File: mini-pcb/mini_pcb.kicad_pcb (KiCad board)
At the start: 4 copper layers, 0 parts

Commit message: mini-pcb layout
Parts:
- added A1: Electrosmith_Daisy_Seed_Rev4, Module:Electrosmith_Daisy_Seed, B.Cu at (122.5, 132.3)
- added C1: 10UF, Capacitor_SMD:C_0805_2012Metric, F.Cu at (111.1, 116.6)
- added C10: 10uf, Capacitor_SMD:C_0805_2012Metric, F.Cu at (139.2, 135.2)
- added C2: 10uf, Capacitor_SMD:C_0805_2012Metric, F.Cu at (153.8, 143.4)
- added C3: 10uf, Capacitor_SMD:C_0805_2012Metric, F.Cu at (163.0, 129.0)
- added C4: 10UF, Capacitor_SMD:C_0805_2012Metric, F.Cu at (111.1, 114.6)
- added C5: 10uf, Capacitor_SMD:C_0805_2012Metric, F.Cu at (168.8, 129.0)
- added C6: 10uf, Capacitor_SMD:C_0805_2012Metric, F.Cu at (153.7, 136.3)
- added C7: 0.1uf, Capacitor_SMD:C_0805_2012Metric, F.Cu at (107.5, 116.6)
- added C8: 0.1uf, Capacitor_SMD:C_0805_2012Metric, F.Cu at (107.5, 114.6)
- added C9: 10uf, Capacitor_SMD:C_0805_2012Metric, F.Cu at (139.2, 144.6)
- added D1: 1N5817, Diode_SMD:D_SOD-123, F.Cu at (105.3, 120.1)
- added J3: Barrel_Jack_Switch, Connector_BarrelJack:BarrelJack_Horizontal, B.Cu at (99.5, 127.8)
- added J4: AUDIO_IN_TRS, Connector_Audio:Jack_6.35mm_Neutrik_NMJ6HCD3_Horizontal, F.Cu at (181.5, 131.8)
- added J5: AUDIO_OUT_TRS, Connector_Audio:Jack_6.35mm_Neutrik_NMJ6HCD3_Horizontal, F.Cu at (111.0, 148.1)
- added R1: 1M, Resistor_SMD:R_0603_1608Metric, F.Cu at (154.2, 138.8)
- added R10: 1M, Resistor_SMD:R_0603_1608Metric, F.Cu at (154.2, 140.9)
- added R11: 1M, Resistor_SMD:R_0603_1608Metric, F.Cu at (162.2, 125.8)
- added R12: 1M, Resistor_SMD:R_0603_1608Metric, F.Cu at (163.8, 125.8)
- added R13: 1M, Resistor_SMD:R_0603_1608Metric, F.Cu at (139.8, 137.8)
- added R14: 1M, Resistor_SMD:R_0603_1608Metric, F.Cu at (137.5, 135.2)
- added R2: 1M, Resistor_SMD:R_0603_1608Metric, F.Cu at (155.5, 136.3)
- added R3: 1M, Resistor_SMD:R_0603_1608Metric, F.Cu at (169.5, 125.8)
- added R4: 1M, Resistor_SMD:R_0603_1608Metric, F.Cu at (168.0, 125.8)
- added R5: 1M, Resistor_SMD:R_0603_1608Metric, F.Cu at (139.8, 142.1)
- added R6: 1M, Resistor_SMD:R_0603_1608Metric, F.Cu at (158.8, 136.0)
- added R7: 1M, Resistor_SMD:R_0603_1608Metric, F.Cu at (158.8, 137.5)
- added R8: 1M, Resistor_SMD:R_0603_1608Metric, F.Cu at (137.5, 144.6)
- added R9: 1M, Resistor_SMD:R_0603_1608Metric, F.Cu at (155.5, 143.4)
- added U1: LM1117DT-5.0, Package_TO_SOT_SMD:TO-252-3_TabPin2, F.Cu at (110.0, 124.1)
- added U2: OPA1664D, Package_SO:SOIC-14_3.9x8.7mm_P1.27mm, F.Cu at (148.5, 140.0)
- added U3: OPA1655DBV, Package_TO_SOT_SMD:SOT-23-5, F.Cu at (158.5, 140.0)
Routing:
- net AUDIO_IN_JACK_RIGHT: track 0.00 -> 75.9 mm
- net AUDIO_OUT_JACK_RIGHT: track 0.00 -> 40.3 mm
- net unconnected-(A1-SPI1_SCK-Pad9): track 0.00 -> 38.4 mm
- net +3.3V: track 38.4 -> 0.00 mm
- net Net-(BT1-+): track 36.6 -> 0.00 mm
- net AUDIO_OUT_JACK_LEFT: track 0.00 -> 29.4 mm
- net AUDIO_IN_JACK_LEFT: track 0.00 -> 29.4 mm
- net +2.5V: track 0.00 -> 10.5 mm
- net DGND: track 0.00 -> 9.58 mm, vias 0 -> 7
- net Net-(U2C--): track 0.00 -> 8.69 mm, vias 0 -> 2
- net Net-(U2D--): track 0.00 -> 8.68 mm
- net +5V: track 0.00 -> 6.78 mm
- net Net-(U2A-+): track 0.00 -> 4.27 mm
- net Net-(U2B-+): track 0.00 -> 4.12 mm
- net Net-(U3-+): track 0.00 -> 3.07 mm
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- added copper zone on In1.Cu, net (none)
- added copper zone on In2.Cu, net (none)
- removed copper zone on In2.Cu, net +3.3V
- removed copper zone on In1.Cu, net GND
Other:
- board outline added: 110 x 22.2 mm

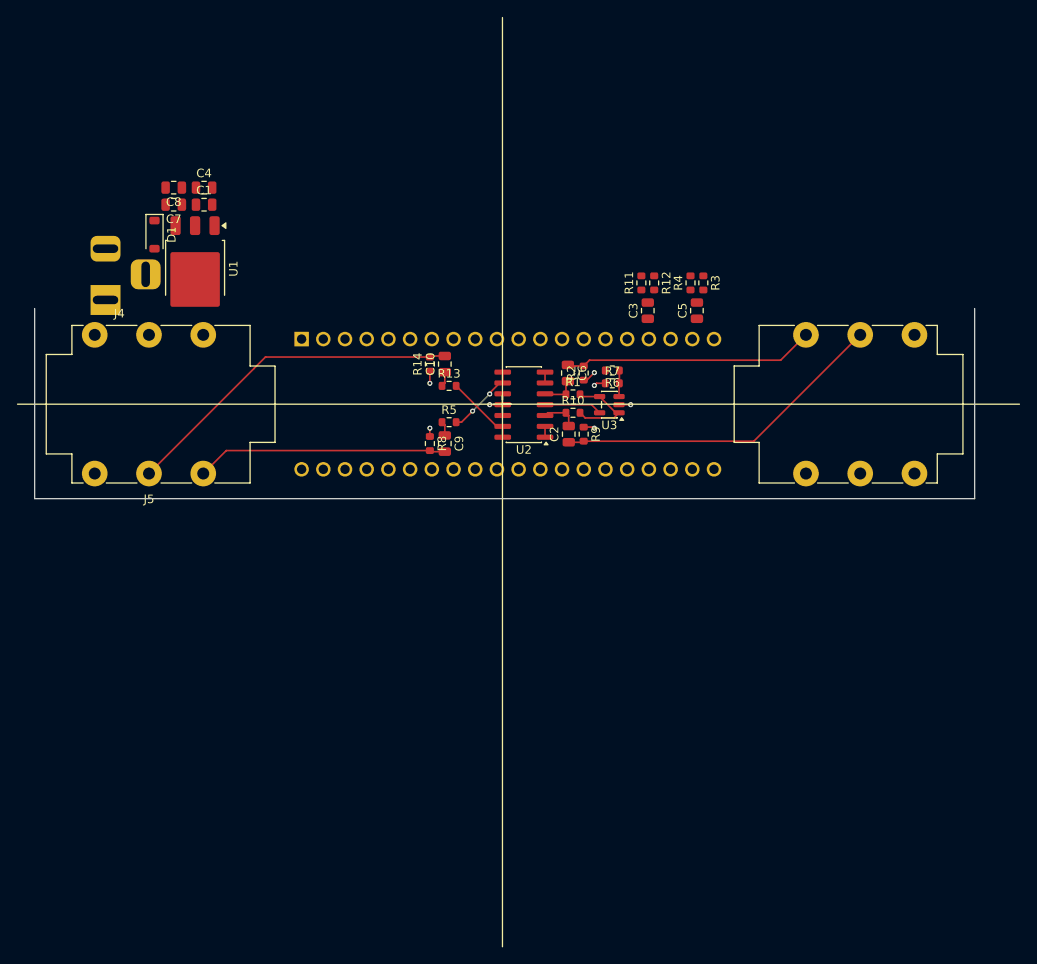
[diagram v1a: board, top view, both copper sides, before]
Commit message: eletronic simulation made
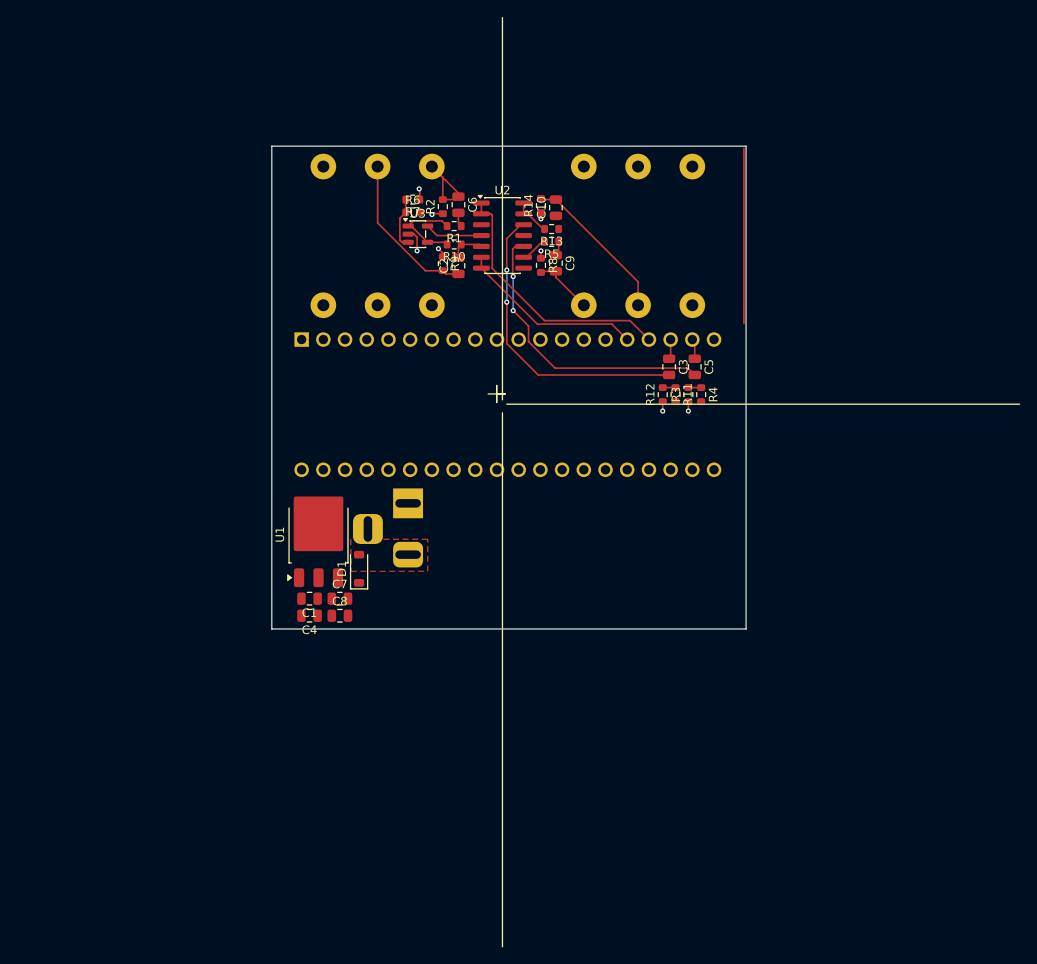
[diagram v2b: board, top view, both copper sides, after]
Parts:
- J4, J5: moved to B.Cu
- moved C8 53.7 mm to (127.0, 164.7), turned to 0 degrees
- moved C4 51.6 mm to (123.4, 164.7), turned to 180 degrees
- moved C7 50.0 mm to (127.0, 162.7), turned to 0 degrees
- moved J5 48.7 mm to (155.5, 128.4), turned to 0 degrees
- moved J4 48.0 mm to (137.7, 112.1), turned to 180 degrees
- moved C1 47.7 mm to (123.4, 162.7), turned to 180 degrees
- moved D1 45.8 mm to (129.2, 159.2), turned to 90 degrees
- moved J3 42.7 mm to (135.0, 151.6), turned to 90 degrees
- moved U1 34.3 mm to (124.5, 155.2), turned to 90 degrees
- moved R7 31.7 mm to (135.5, 116.0), turned to 180 degrees
- moved U3 30.0 mm to (136.1, 120.0), turned to 0 degrees
- moved R6 29.8 mm to (135.5, 117.5), turned to 0 degrees
- moved R9 25.9 mm to (139.0, 123.5)
- moved R2 25.5 mm to (139.0, 116.8)
- moved C9 24.8 mm to (152.2, 123.5)
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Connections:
- C2 pad 2: Net-(U2A-+) -> Net-(U2B-+)
- C6 pad 2: Net-(U2B-+) -> Net-(U2A-+)
- R1 pad 1: Net-(U2B-+) -> Net-(U2A-+)
- R10 pad 1: Net-(U2A-+) -> Net-(U2B-+)
- U2 pad 1: AUDIO_IN_JACK_RIGHT_BUF -> AUDIO_IN_JACK_LEFT_BUF
- U2 pad 2: AUDIO_IN_JACK_RIGHT_BUF -> AUDIO_IN_JACK_LEFT_BUF
- U2 pad 6: AUDIO_IN_JACK_LEFT_BUF -> AUDIO_IN_JACK_RIGHT_BUF
- U2 pad 7: AUDIO_IN_JACK_LEFT_BUF -> AUDIO_IN_JACK_RIGHT_BUF
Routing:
- net Net-(U2D-+): track 0.00 -> 37.0 mm, vias 0 -> 2
- net Net-(U2C-+): track 0.00 -> 35.6 mm, vias 0 -> 2
- net AUDIO_IN_JACK_LEFT_BUF: track 1.27 -> 30.6 mm
- net AUDIO_OUT_JACK_LEFT: track 29.4 -> 7.12 mm
- net AUDIO_OUT_JACK_RIGHT: track 40.3 -> 18.1 mm
- net AUDIO_IN_JACK_RIGHT: track 75.9 -> 55.1 mm
- net AUDIO_IN_JACK_RIGHT_BUF: track 1.27 -> 21.8 mm
- net AUDIO_IN_JACK_LEFT: track 29.4 -> 11.2 mm
- net Net-(U2C--): track 8.69 -> 3.20 mm, vias 2 -> 0
- net Net-(U2D--): track 8.68 -> 4.46 mm
- net Net-(U3-+): track 3.07 -> 6.10 mm
- net Net-(U2A-+): track 4.27 -> 1.68 mm
- net AUDIO_OUT_JACK_LEFT_BUF: track 0.00 -> 2.36 mm
- net AUDIO_OUT_JACK_RIGHT_BUF: track 0.00 -> 2.32 mm
- net Net-(C10-Pad1): track 1.73 -> 0.00 mm
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- added copper zone on F.Cu, net POWER_JACK_PWR
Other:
- board size 110 x 22.2 mm -> 55.5 x 56.5 mm

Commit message: pcb update
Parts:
- added J1: Screw_Terminal_01x02, TerminalBlock:TerminalBlock_Xinya_XY308-2.54-2P_1x02_P2.54mm_Horizontal, F.Cu at (144.7, 165.7)
- added U4: ESP32-C3-WROOM-02, RF_Module:ESP32-C3-WROOM-02, F.Cu at (161.1, 159.9)
- moved C1 42.2 mm to (144.2, 126.0)
- moved U1 11.6 mm to (134.2, 161.5), turned to -90 degrees
- moved J3 8.98 mm to (126.0, 152.2)
- moved R6 6.79 mm to (134.8, 124.2)
- moved R7 6.79 mm to (134.8, 122.8)
- moved R5 3.31 mm to (151.6, 124.2)
- moved R8 3.13 mm to (151.6, 120.8), turned to 0 degrees
- moved C4 2.94 mm to (122.2, 162.0), turned to -90 degrees
- moved C8 2.70 mm to (126.8, 162.0), turned to -90 degrees
- moved C7 2.57 mm to (124.5, 162.0), turned to -90 degrees
- moved R2 1.83 mm to (140.5, 115.8), turned to 180 degrees
- moved R9 1.66 mm to (140.5, 124.2), turned to 180 degrees
- moved R11 1.51 mm to (164.8, 139.0)
- moved R12 1.51 mm to (166.2, 139.0)
- moved R14 1.47 mm to (151.6, 115.8), turned to 0 degrees
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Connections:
- A1 pad 28: unconnected-(A1-ADC_6-Pad28) -> Net-(A1-ADC_6)
- J4 pad S: GND -> GNDA
- J5 pad S: GND -> GNDA
- R12 pad 1: DGND -> AGND
- R14 pad 1: DGND -> AGND
- R2 pad 1: DGND -> AGND
- R3 pad 1: DGND -> AGND
- R7 pad 1: DGND -> AGND
- R8 pad 1: DGND -> AGND
- R9 pad 1: DGND -> AGND
- U3 pad 2: DGND -> AGND
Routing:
- net +5V: track 6.75 -> 120.9 mm
- net Net-(U2D-+): track 37.0 -> 4.35 mm, vias 2 -> 0
- net Net-(U2C-+): track 35.6 -> 4.35 mm, vias 2 -> 0
- net AUDIO_IN_JACK_RIGHT: track 55.1 -> 38.4 mm
- net +9V: track 0.00 -> 11.9 mm
- net DGND: track 10.3 -> 0.00 mm, vias 8 -> 0
- net AUDIO_IN_JACK_LEFT: track 11.2 -> 6.52 mm
- net POWER_JACK_PWR: track 0.00 -> 3.68 mm
- net Net-(U2A-+): track 1.68 -> 5.00 mm
- net Net-(U3-+): track 6.10 -> 3.08 mm
- net Net-(C10-Pad1): track 0.00 -> 2.50 mm
- net AUDIO_OUT_JACK_RIGHT: track 18.1 -> 16.3 mm
- net AUDIO_OUT_JACK_LEFT: track 7.12 -> 8.70 mm
- net Net-(U2B-+): track 4.14 -> 5.00 mm
- net Net-(C9-Pad1): track 1.68 -> 2.50 mm
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- added copper zone on B.Cu, net AGND
- added copper zone on F.Cu, net AGND
- removed copper zone on F.Cu, net POWER_JACK_PWR
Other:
- board size 55.5 x 56.5 mm -> 57 x 60.5 mm

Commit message: almost done with mini pcb
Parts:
- removed U4: ESP32-C3-WROOM-02, RF_Module:ESP32-C3-WROOM-02
- added R15: 10k, Resistor_SMD:R_0603_1608Metric, F.Cu at (142.5, 112.5)
- added R16: 39k, Resistor_SMD:R_0603_1608Metric, F.Cu at (142.5, 114.0)
- added R17: 10k, Resistor_SMD:R_0603_1608Metric, F.Cu at (142.5, 128.0)
- added R18: 39k, Resistor_SMD:R_0603_1608Metric, F.Cu at (142.5, 126.5)
- added R19: 39k, Resistor_SMD:R_0603_1608Metric, F.Cu at (151.0, 127.0)
- added R20: 10k, Resistor_SMD:R_0603_1608Metric, F.Cu at (151.0, 128.5)
- J1: moved to B.Cu
- R13, R14: value 1M -> 100
- R5: value 1M -> 10k
- R8: value 1M -> 39k
- moved C1 29.4 mm to (135.2, 154.0), turned to 0 degrees
- moved R14 13.4 mm to (144.8, 127.2), turned to -90 degrees
- moved R8 9.27 mm to (151.0, 130.0)
- moved R13 8.01 mm to (145.5, 114.0), turned to 0 degrees
- moved J1 2.55 mm to (147.3, 165.7), turned to 180 degrees
- moved C10 1.88 mm to (152.9, 118.8)
- moved C9 1.59 mm to (152.9, 121.8)
- moved R5 1.37 mm to (151.0, 125.5), turned to 0 degrees
- moved C2 1.25 mm to (139.5, 123.2)
- moved R10 1.25 mm to (139.5, 121.5)
- moved R9 1.25 mm to (139.5, 125.0)
- moved C6 1.03 mm to (139.5, 117.2)
- moved R1 1.03 mm to (139.5, 119.0)
- moved R2 1.03 mm to (139.5, 115.5)
- moved R6 1.00 mm to (133.8, 124.2)
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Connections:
- A1 pad 20: GNDA -> GND
- A1 pad 40: DGND -> GND
- C10 pad 1: Net-(C10-Pad1) -> Net-(U2D--)
- C3 pad 2: Net-(U2D-+) -> Net-(C3-Pad2)
- C5 pad 2: Net-(U2C-+) -> Net-(C5-Pad2)
- C9 pad 1: Net-(C9-Pad1) -> Net-(U2C--)
- J4 pad S: GNDA -> GND
- J5 pad S: GNDA -> GND
- R11 pad 1: Net-(U2D-+) -> Net-(C3-Pad2)
- R12 pad 1: AGND -> GND
- R12 pad 2: Net-(U2D-+) -> Net-(C3-Pad2)
- R13 pad 1: Net-(C10-Pad1) -> Net-(R13-Pad1)
- R13 pad 2: Net-(U2D--) -> AUDIO_IN_JACK_LEFT_BUF
- R14 pad 1: AGND -> Net-(R14-Pad1)
- R14 pad 2: AUDIO_OUT_JACK_RIGHT -> AUDIO_IN_JACK_RIGHT_BUF
- R2 pad 1: AGND -> GND
- R3 pad 1: AGND -> GND
- R3 pad 2: Net-(U2C-+) -> Net-(C5-Pad2)
- R4 pad 1: Net-(U2C-+) -> Net-(C5-Pad2)
- R5 pad 1: Net-(C9-Pad1) -> Net-(U2C-+)
- R5 pad 2: Net-(U2C--) -> GND
- R7 pad 1: AGND -> GND
- R8 pad 1: AGND -> Net-(U2D-+)
- R8 pad 2: AUDIO_OUT_JACK_LEFT -> Net-(C3-Pad2)
- R9 pad 1: AGND -> GND
- U2 pad 1: AUDIO_IN_JACK_LEFT_BUF -> Net-(R13-Pad1)
- U2 pad 11: DGND -> GND
- U2 pad 2: AUDIO_IN_JACK_LEFT_BUF -> Net-(U2A--)
- U2 pad 6: AUDIO_IN_JACK_RIGHT_BUF -> Net-(U2B--)
- U2 pad 7: AUDIO_IN_JACK_RIGHT_BUF -> Net-(R14-Pad1)
- U3 pad 2: AGND -> GND
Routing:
- net +3.3VD: track 0.00 -> 55.1 mm
- net unconnected-(A1-SPI1_SCK-Pad9): track 38.4 -> 0.00 mm
- net +5V: track 120.9 -> 91.1 mm, vias 0 -> 4
- net Net-(C5-Pad2): track 0.00 -> 27.5 mm
- net Net-(C3-Pad2): track 0.00 -> 23.0 mm
- net Net-(A1-ADC_6): track 0.00 -> 21.5 mm
- net AUDIO_IN_JACK_RIGHT: track 38.4 -> 23.1 mm
- net GND: track 0.00 -> 15.2 mm, vias 0 -> 41
- net +9V: track 11.9 -> 24.3 mm
- net Net-(U2D-+): track 4.35 -> 14.3 mm
- net Net-(U2A--): track 0.00 -> 6.55 mm
- net Net-(U2B--): track 0.00 -> 6.18 mm
- net Net-(R13-Pad1): track 0.00 -> 5.19 mm
- net Net-(U2C-+): track 4.35 -> 8.66 mm
- net Net-(R14-Pad1): track 0.00 -> 4.26 mm
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- added copper zone on B.Cu, net GND
- added copper zone on F.Cu, net GND
- removed copper zone on In1.Cu, net (none)
- removed copper zone on In2.Cu, net (none)
- removed copper zone on B.Cu, net AGND
- removed copper zone on F.Cu, net AGND
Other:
- copper layers 4 -> 2
- board text added: "Install 2 2.54mm 1x20 female pin headers for A1"

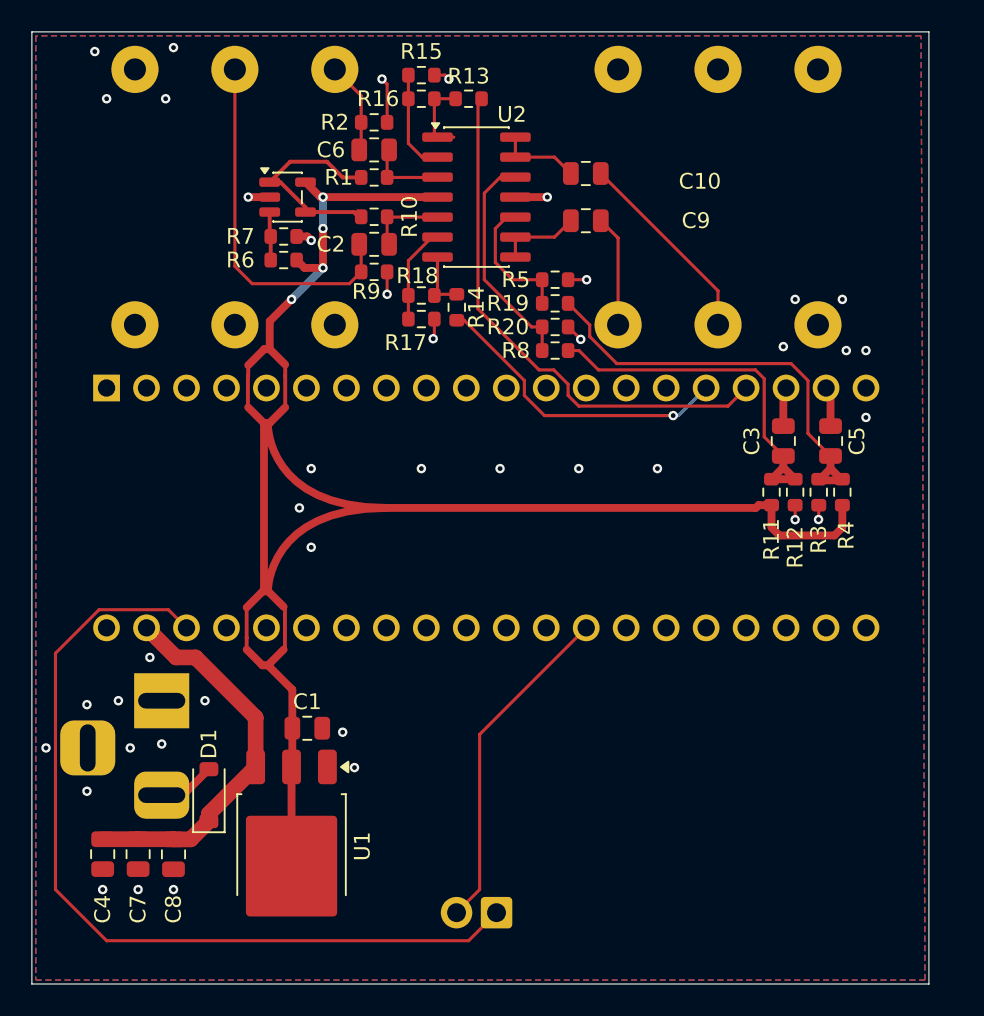
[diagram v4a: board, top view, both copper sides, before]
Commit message: made final touches and bom still needs through testing
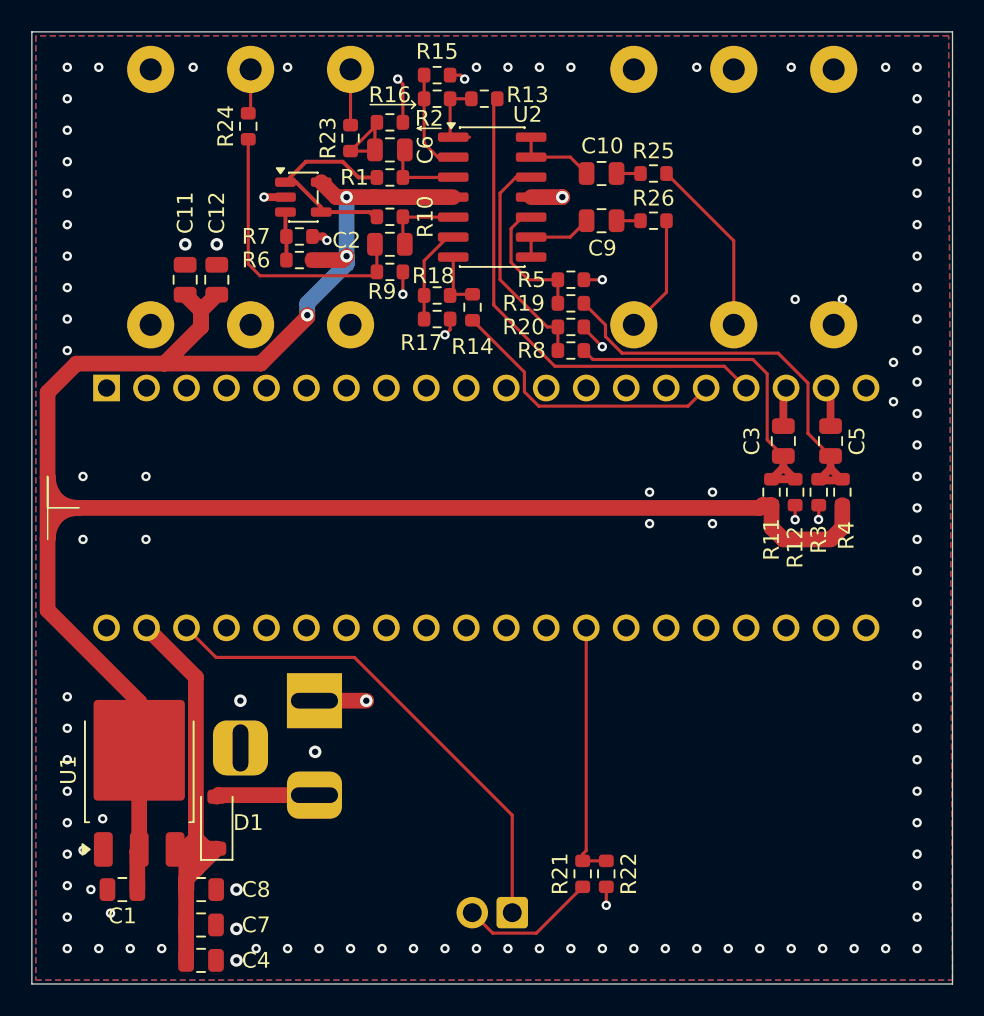
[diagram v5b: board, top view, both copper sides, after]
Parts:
- added C11: 0.1uf, Capacitor_SMD:C_0805_2012Metric, F.Cu at (127.5, 125.5)
- added C12: 0.1uf, Capacitor_SMD:C_0805_2012Metric, F.Cu at (129.5, 125.5)
- added R21: 100, Resistor_SMD:R_0603_1608Metric, F.Cu at (152.8, 163.2)
- added R22: 10k, Resistor_SMD:R_0603_1608Metric, F.Cu at (154.2, 163.2)
- added R23: 100k, Resistor_SMD:R_0603_1608Metric, F.Cu at (138.0, 116.5)
- added R24: 100k, Resistor_SMD:R_0603_1608Metric, F.Cu at (131.5, 115.8)
- added R25: 1k, Resistor_SMD:R_0603_1608Metric, F.Cu at (157.2, 118.8)
- added R26: 1k, Resistor_SMD:R_0603_1608Metric, F.Cu at (157.2, 121.8)
- moved C1 15.6 mm to (123.5, 164.2), turned to 180 degrees
- moved U1 10.8 mm to (124.6, 156.7), turned to 90 degrees
- moved J3 9.71 mm to (135.7, 152.2)
- moved C4 9.20 mm to (128.5, 168.8), turned to 0 degrees
- moved C7 6.02 mm to (128.5, 166.5), turned to 0 degrees
- moved C8 2.85 mm to (128.5, 164.2), turned to 0 degrees
- moved D1 1.82 mm to (129.5, 160.0)
- moved C10 1.00 mm to (153.9, 118.8)
- moved C2 1.00 mm to (140.5, 123.2)
- moved C6 1.00 mm to (140.5, 117.2)
- moved C9 1.00 mm to (153.9, 121.8)
- moved J1 1.00 mm to (148.3, 165.7)
- moved J4 1.00 mm to (138.0, 112.1)
- moved J5 1.00 mm to (156.0, 128.4)
- moved R1 1.00 mm to (140.5, 119.0)
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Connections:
- C10 pad 2: AUDIO_OUT_JACK_RIGHT -> Net-(C10-Pad2)
- C2 pad 1: AUDIO_IN_JACK_RIGHT -> Net-(C2-Pad1)
- C6 pad 1: AUDIO_IN_JACK_LEFT -> Net-(C6-Pad1)
- C9 pad 2: AUDIO_OUT_JACK_LEFT -> Net-(C9-Pad2)
- J1 pad 2: Net-(A1-ADC_6) -> Net-(J1-Pin_2)
- R2 pad 2: AUDIO_IN_JACK_LEFT -> Net-(C6-Pad1)
- R9 pad 2: AUDIO_IN_JACK_RIGHT -> Net-(C2-Pad1)
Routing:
- net +5V: track 91.1 -> 133.0 mm, vias 4 -> 3
- net +3.3VD: track 55.1 -> 31.8 mm
- net AUDIO_IN_JACK_RIGHT: track 23.1 -> 2.85 mm
- net Net-(C2-Pad1): track 0.00 -> 18.4 mm
- net Net-(J1-Pin_2): track 0.00 -> 8.77 mm
- net +9V: track 24.3 -> 30.6 mm
- net Net-(C6-Pad1): track 0.00 -> 5.90 mm
- net Net-(A1-ADC_6): track 21.5 -> 16.4 mm
- net GND: track 15.2 -> 20.1 mm, vias 41 -> 118
- net POWER_JACK_PWR: track 3.68 -> 6.25 mm
- net AUDIO_IN_JACK_LEFT_BUF: track 34.3 -> 31.7 mm
- net AUDIO_IN_JACK_LEFT: track 5.86 -> 3.54 mm
- net Net-(C9-Pad2): track 0.00 -> 1.53 mm
- net Net-(C10-Pad2): track 0.00 -> 1.53 mm
- net AUDIO_IN_JACK_RIGHT_BUF: track 19.6 -> 18.3 mm, vias 1 -> 0
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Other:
- board size 57 x 60.5 mm -> 58.5 x 60.5 mm
